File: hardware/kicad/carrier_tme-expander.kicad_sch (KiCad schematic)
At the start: 9 parts, among them U2 TCA9534PWR

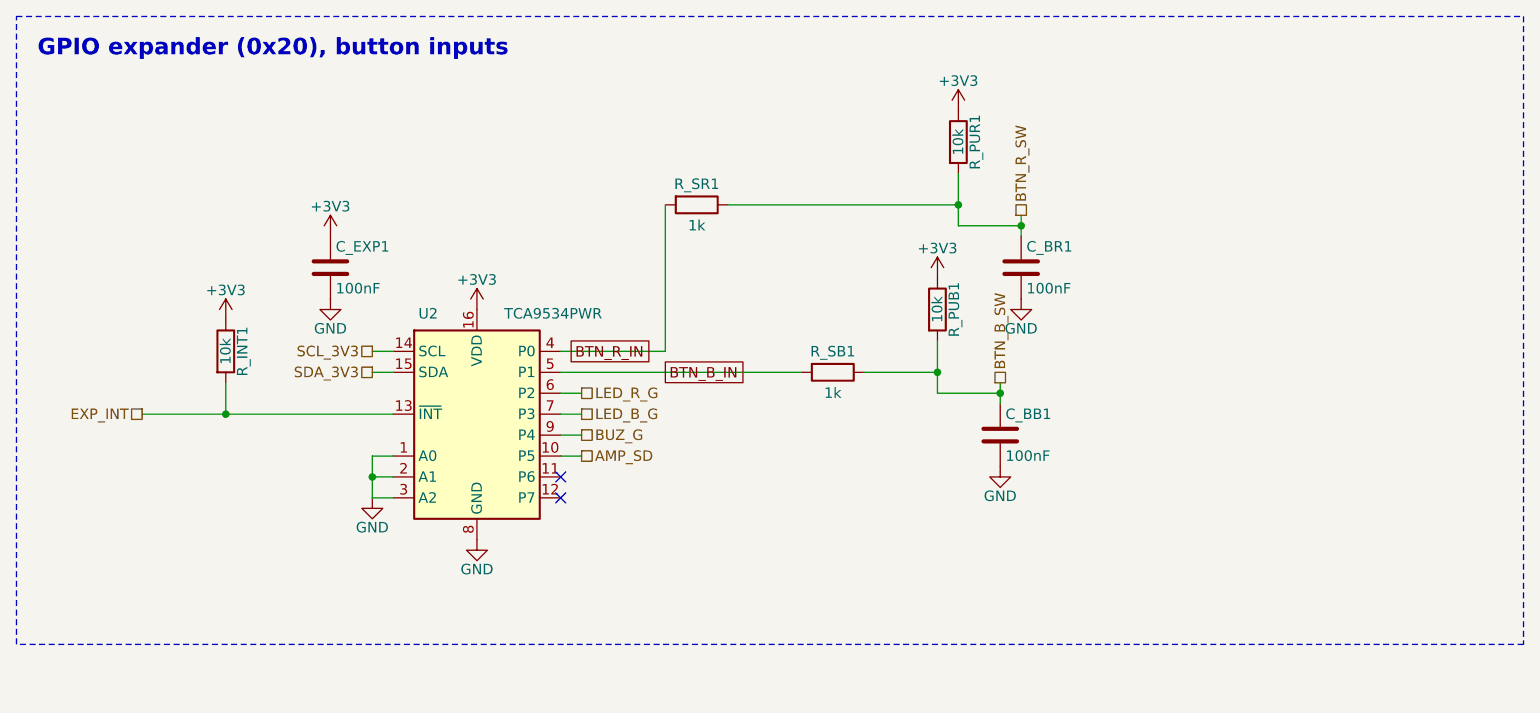
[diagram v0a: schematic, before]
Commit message: hardware: carrier_tme schematic: cables, root board-edge parts, review clean
Review (Konnect, audits each sheet on its own): 20 errors -> 0.
- Off-board parts are virtual #X_* symbols (out of the netlist and BOMs).
- Board-edge parts are drawn on the root beside their connectors: the
  power-entry caps, the debug headers and test pads, D_FLY1 (across the
  buzzer) and the I2C level shifter with the bus pull-ups. Every rail on the
  root has its bulk cap there; the i2c, power and debug sheets are gone
  (function sheets: expander, drivers, audio).
- J2 pin 2 is "CHG IN" (a 5V name read as an undecoupled supply pin).

Cables: root connectors and off-board modules use 5.08 mm-pitch symbols
(local:Conn_W_02/04/06, recreated module symbols; footprints unchanged).
Every off-board pin is wired to its connector pin; a rail's power port hangs
off its cable (gen_sch cable + tee_port, drawn after the signals). 2.54 mm
headers keep ports along their stubs (ROOT port_modes).

Leftover gaps: gen_sch fits each function block to its content.

make BOARD=carrier_tme all: netlist matches, ERC 0, DRC 0/0/0 parity,
gerbers ok; board changed only in footprint paths and J2's unconnected net
name. Flat boards regenerate byte-identical. Remaining review warnings: MPN,
U2 pull-ups and expander bulk (both on the root sheet).

Co-Authored-By: Claude Opus 5.5 <noreply@anthropic.com>
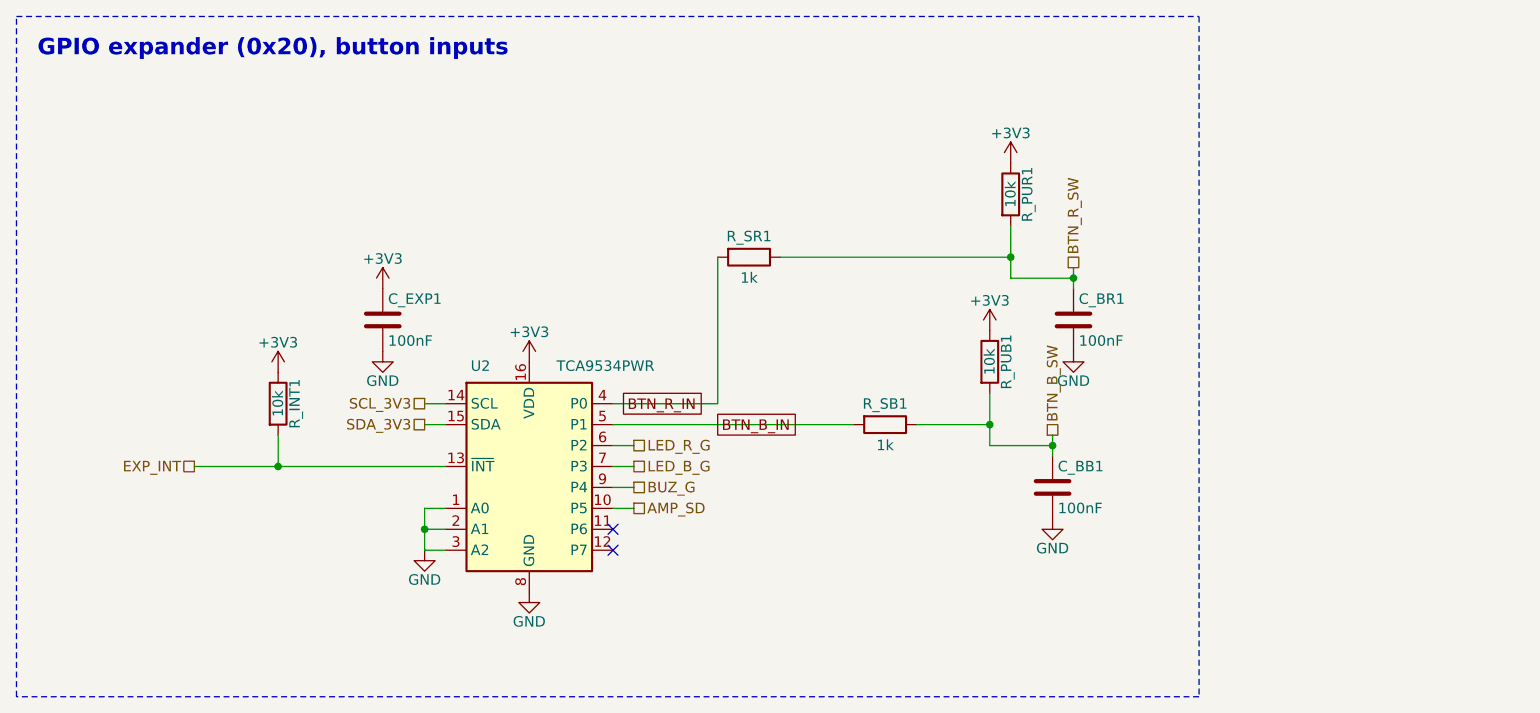
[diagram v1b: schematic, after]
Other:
- moved on the sheet: C_BB1, C_BR1, C_EXP1, R_INT1, R_PUB1, R_PUR1, R_SB1, R_SR1, U2
